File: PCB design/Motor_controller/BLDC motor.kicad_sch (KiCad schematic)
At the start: 25 parts, among them J11 532610371, J12 1984620, U13 DRV8311H

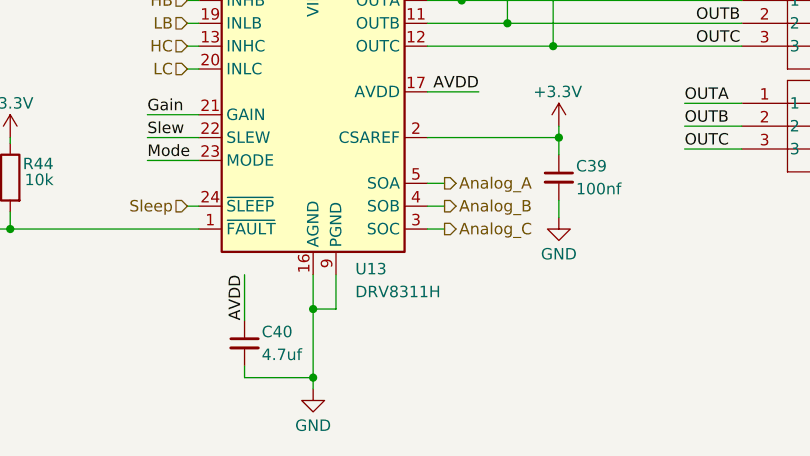
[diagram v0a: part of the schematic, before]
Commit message: modified:   .vscode/Motor_controller.mplab.json 	new file:   Firmware/Doxyfile 	modified:   Firmware/Motor_controller.X/Motor_controller_default/components/FreeRTOS.yml 	modified:   Firmware/Motor_controller.X/Motor_controller_default/components/I2C/I2C.yml 	modified:   Firmware/Motor_controller.X/Motor_controller_default/components/I2C/components/sercom1.yml 	modified:   Firmware/Motor_controller.X/Motor_controller_default/components/Servo Motor/components/sercom4.yml 	deleted:    Firmware/Motor_controller.X/Motor_controller_default/components/X2Cscope.yml 	modified:   Firmware/Motor_controller.X/Motor_controller_default/components/adc0.yml 	modified:   Firmware/Motor_controller.X/Motor_controller_default/components/core.yml 	modified:   Firmware/Motor_controller.X/Motor_controller_default/components/evsys.yml 	modified:   Firmware/Motor_controller.X/Motor_controller_default/components/nvmctrl.yml 	modified:   Firmware/Motor_controller.X/Motor_controller_default/components/pmsm_foc.yml 	modified:   Firmware/Motor_controller.X/Motor_controller_default/components/pmsm_motor.yml 	modified:   Firmware/Motor_controller.X/Motor_controller_default/components/sercom3.yml 	modified:   Firmware/Motor_controller.X/Motor_controller_default/components/tcc0.yml 	modified:   Firmware/Motor_controller.X/Motor_controller_default/mcc-config.mc4 	modified:   Firmware/Motor_controller.X/mcc-manifest-autosave.yml 	modified:   Firmware/Motor_controller.X/mcc-manifest-generated-success.yml 	new file:   Firmware/src/BLDC/FOC_ADC.c 	new file:   Firmware/src/BLDC/FOC_ADC.h 	new file:   Firmware/src/BLDC/FOC_PWM.c 	new file:   Firmware/src/BLDC/FOC_PWM.h 	new file:   Firmware/src/BLDC/FOC_utilities.c 	new file:   Firmware/src/BLDC/FOC_utilities.h 	modified:   Firmware/src/config/default/QSpin/Field_Oriented_Control/mc_field_oriented_control.c 	modified:   Firmware/src/config/default/QSpin/Field_Oriented_Control/mc_field_oriented_control.h 	modified:   Firmware/src/config/default/QSpin/Field_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
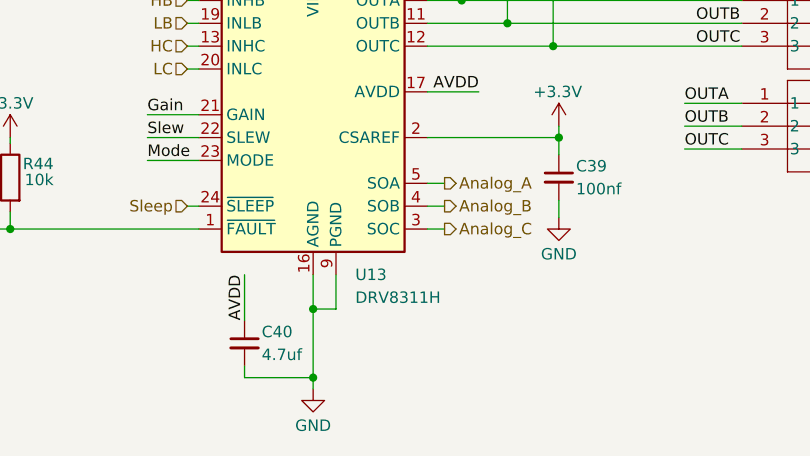
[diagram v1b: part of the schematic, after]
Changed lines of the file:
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@@
 		(fields_autoplaced yes)
 		(property "Reference" "U13"
-			(at 83.4233 107.315 0)
+			(at 83.4233 107.95 0)
 			(show_name no)
 			(do_not_autoplace no)
@@
 		)
 		(property "Value" "DRV8311H"
-			(at 83.4233 109.855 0)
+			(at 83.4233 110.49 0)
 			(show_name no)
 			(do_not_autoplace no)

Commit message: Implemented FOC controller
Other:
- note added: "3 Phase BLDC motor driver"
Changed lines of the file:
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@@
 	(generator_version "10.0")
 	(paper "A4")
+	(text "3 Phase BLDC motor driver"
+		(exclude_from_sim no)
+		(at 93.853 21.336 0)
+		(effects
+			(font
+				(size 7.62 7.62)
+				(thickness 1.524)
+				(bold yes)
+				(color 0 0 0 1)
+			)
+		)
+	)
 	(junction
 		(at 167.005 98.425)
